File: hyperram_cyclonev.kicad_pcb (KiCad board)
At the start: 2 copper layers, 69 parts, among them IC1 AP63205WU, IC2 TXB0108PWR, IC3 S26KL128SDABHI020, IC4 W25Q32JVSSIQ_TR, IC5 S27KL0641DABHI020, J1 ASP-122952-01, J2 HDMI_A, J3 1156915, J4 1156915, J5 Conn_02x06_Top_Bottom, J6 Conn_02x06_Top_Bottom, J7 Conn_02x06_Top_Bottom, J8 1156915, J9 1156915, Q1 BSS138, Q2 BSS138

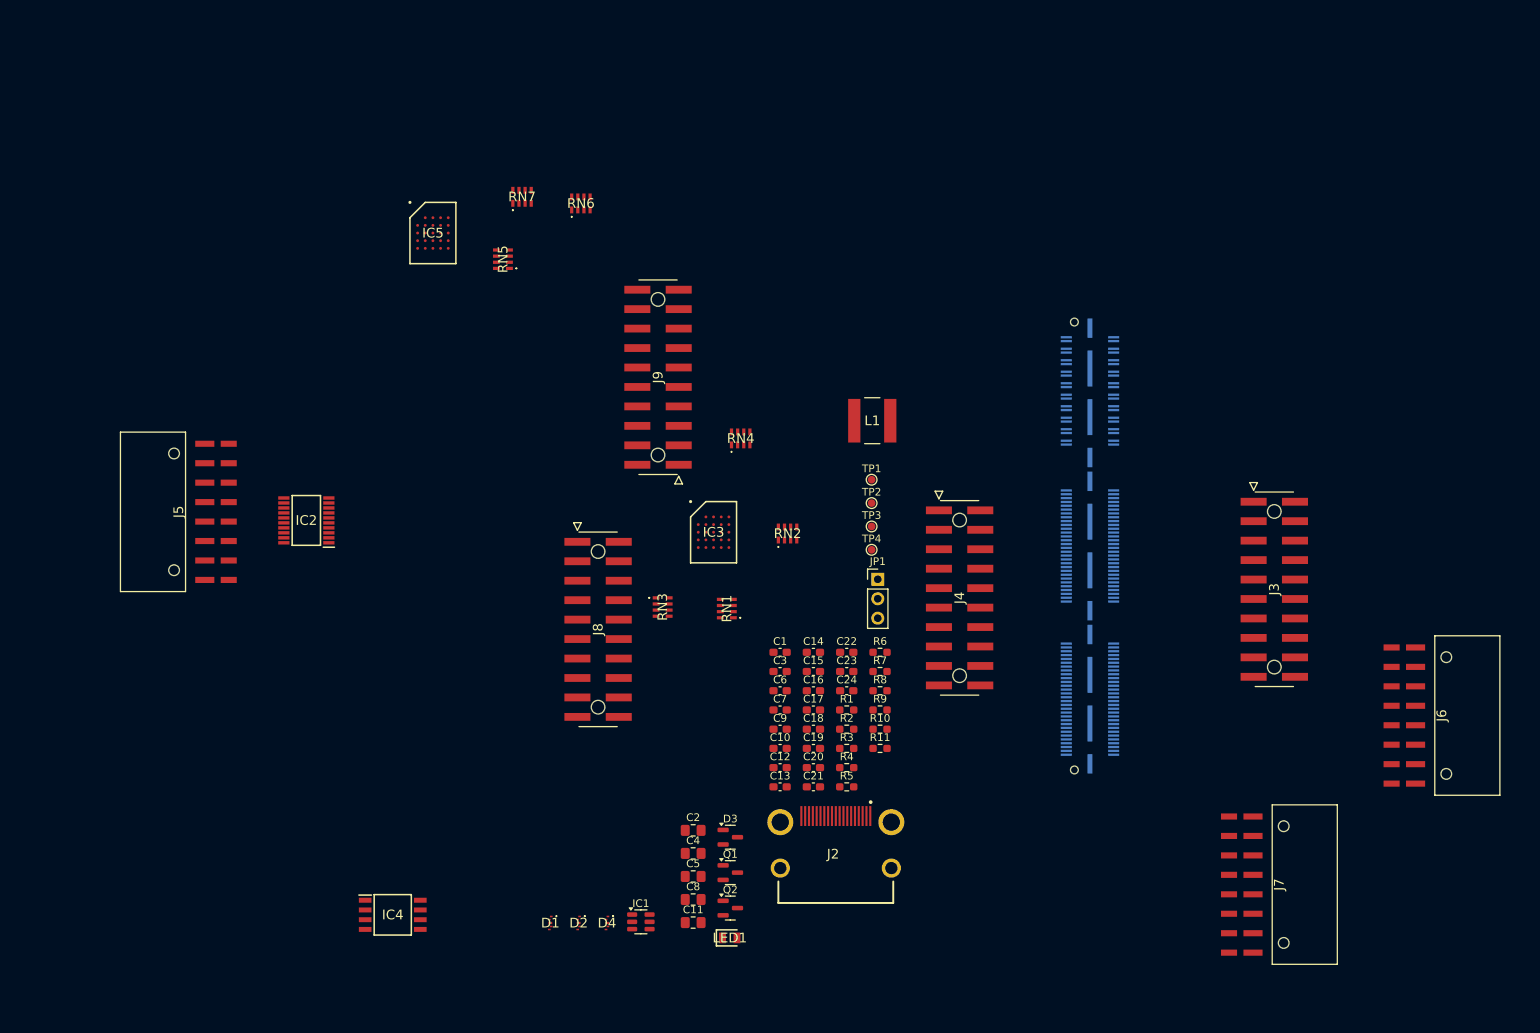
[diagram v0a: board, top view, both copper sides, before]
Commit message: Created edge.cuts. Updated PCB from schematic.
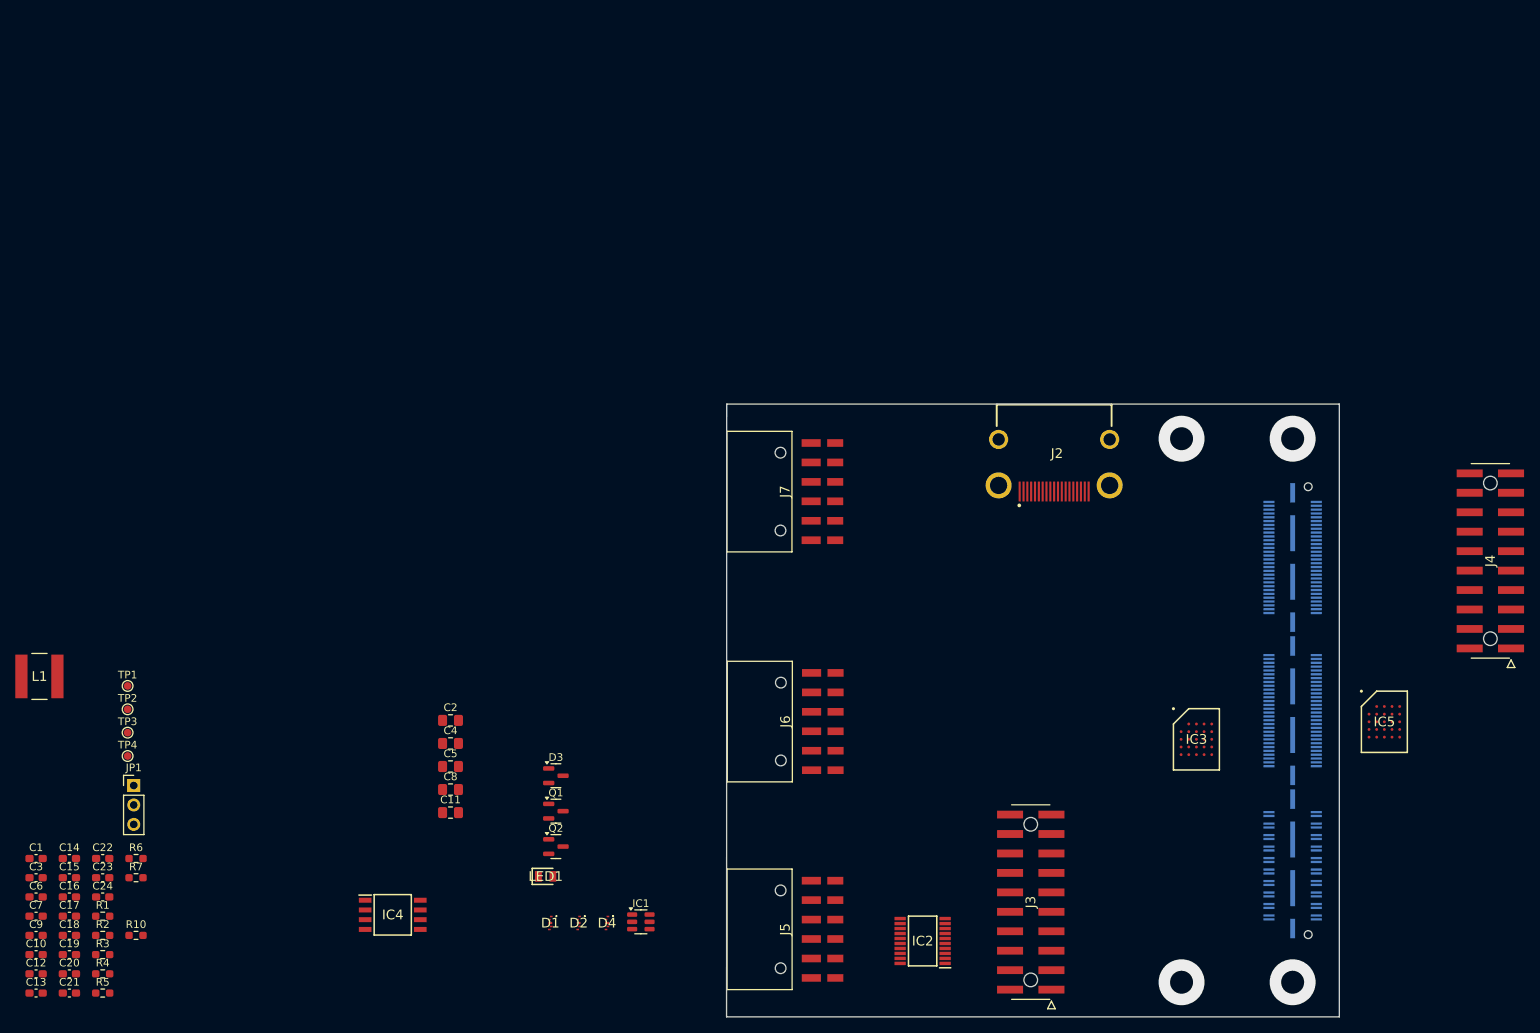
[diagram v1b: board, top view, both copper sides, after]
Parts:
- removed J8, J9: 1156915, hyperram_cyclonev:1156915
- removed R11, R8, R9: R, Resistor_SMD:R_0603_1608Metric_Pad0.98x0.95mm_HandSolder
- removed RN1, RN2, RN3, RN4, RN5, RN6, RN7: CAY16-22R0F4LF, hyperram_cyclonev:CAY16000J4LF
- moved IC5 139.7 mm to (234.5, 114.6)
- moved L1 113.7 mm to (58.9, 108.7)
- moved C1 100.8 mm to (58.4, 132.5)
- moved C10 100.8 mm to (58.4, 145.0)
- moved C12 100.8 mm to (58.4, 147.5)
- moved C13 100.8 mm to (58.4, 150.1)
- moved C14 100.8 mm to (62.8, 132.5)
- moved C15 100.8 mm to (62.8, 135.0)
- moved C16 100.8 mm to (62.8, 137.5)
- moved C17 100.8 mm to (62.8, 140.0)
- moved C18 100.8 mm to (62.8, 142.5)
- moved C19 100.8 mm to (62.8, 145.0)
- moved C20 100.8 mm to (62.8, 147.5)
- moved C21 100.8 mm to (62.8, 150.1)
- moved C22 100.8 mm to (67.1, 132.5)
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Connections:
- J1 pad 41: /cv_hf_csn -> /hf_csn
- J1 pad 42: /cv_hr2_csn -> /hr2_csn
- J1 pad 43: /cv_hr2_rstn -> /hr2_rstn
- J1 pad 44: /cv_hr2_rwds -> /hr2_rwds
- J1 pad 47: /cv_hf_rston -> /hf_rston
- J1 pad 48: /cv_hr2_dq7 -> /hr2_dq7
- J1 pad 49: /cv_hf_intn -> /hf_intn
- J1 pad 50: /cv_hr2_dq6 -> /hr2_dq6
- J1 pad 53: /cv_hr1_csn -> /hr1_csn
- J1 pad 54: /cv_hr2_dq5 -> /hr2_dq5
- J1 pad 55: /cv_hr1_rwds -> /hr1_rwds
- J1 pad 56: /cv_hr2_dq4 -> /hr2_dq4
- J1 pad 59: /cv_hr1_dq7 -> /hr1_dq7
- J1 pad 60: /cv_hr2_dq3 -> /hr2_dq3
- J1 pad 61: /cv_hr1_dq6 -> /hr1_dq6
- J1 pad 62: /cv_hr2_dq2 -> /hr2_dq2
- J1 pad 65: /cv_hr1_dq5 -> /hr1_dq5
- J1 pad 66: /cv_hr2_dq1 -> /hr2_dq1
- J1 pad 67: /cv_hr1_dq4 -> /hr1_dq4
- J1 pad 68: /cv_hr2_dq0 -> /hr2_dq0
- J1 pad 71: /cv_hr1_dq3 -> /hr1_dq3
- J1 pad 72: /cv_hr2_clkp -> /hr2_clkp
- J1 pad 73: /cv_hr1_dq2 -> /hr1_dq2
- J1 pad 74: /cv_hr2_clkn -> /hr2_clkn
- J1 pad 77: /cv_hr1_dq1 -> /hr1_dq1
- J1 pad 78: /cv_hf_psc -> /hf_psc
- J1 pad 79: /cv_hr1_dq0 -> /hr1_dq0
- J1 pad 80: /cv_hf_pscn -> /hf_pscn
- J1 pad 83: /cv_hr1_clkp -> /hr1_clkp
- J1 pad 85: /cv_hr1_clkn -> /hr1_clkn
- J1 pad 89: /cv_hr1_rstn -> /hr1_rstn
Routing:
- net (no net): vias 0 -> 4
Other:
- board outline added: 80 x 80 mm

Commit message: Fixed issue with PMOD pins assignment
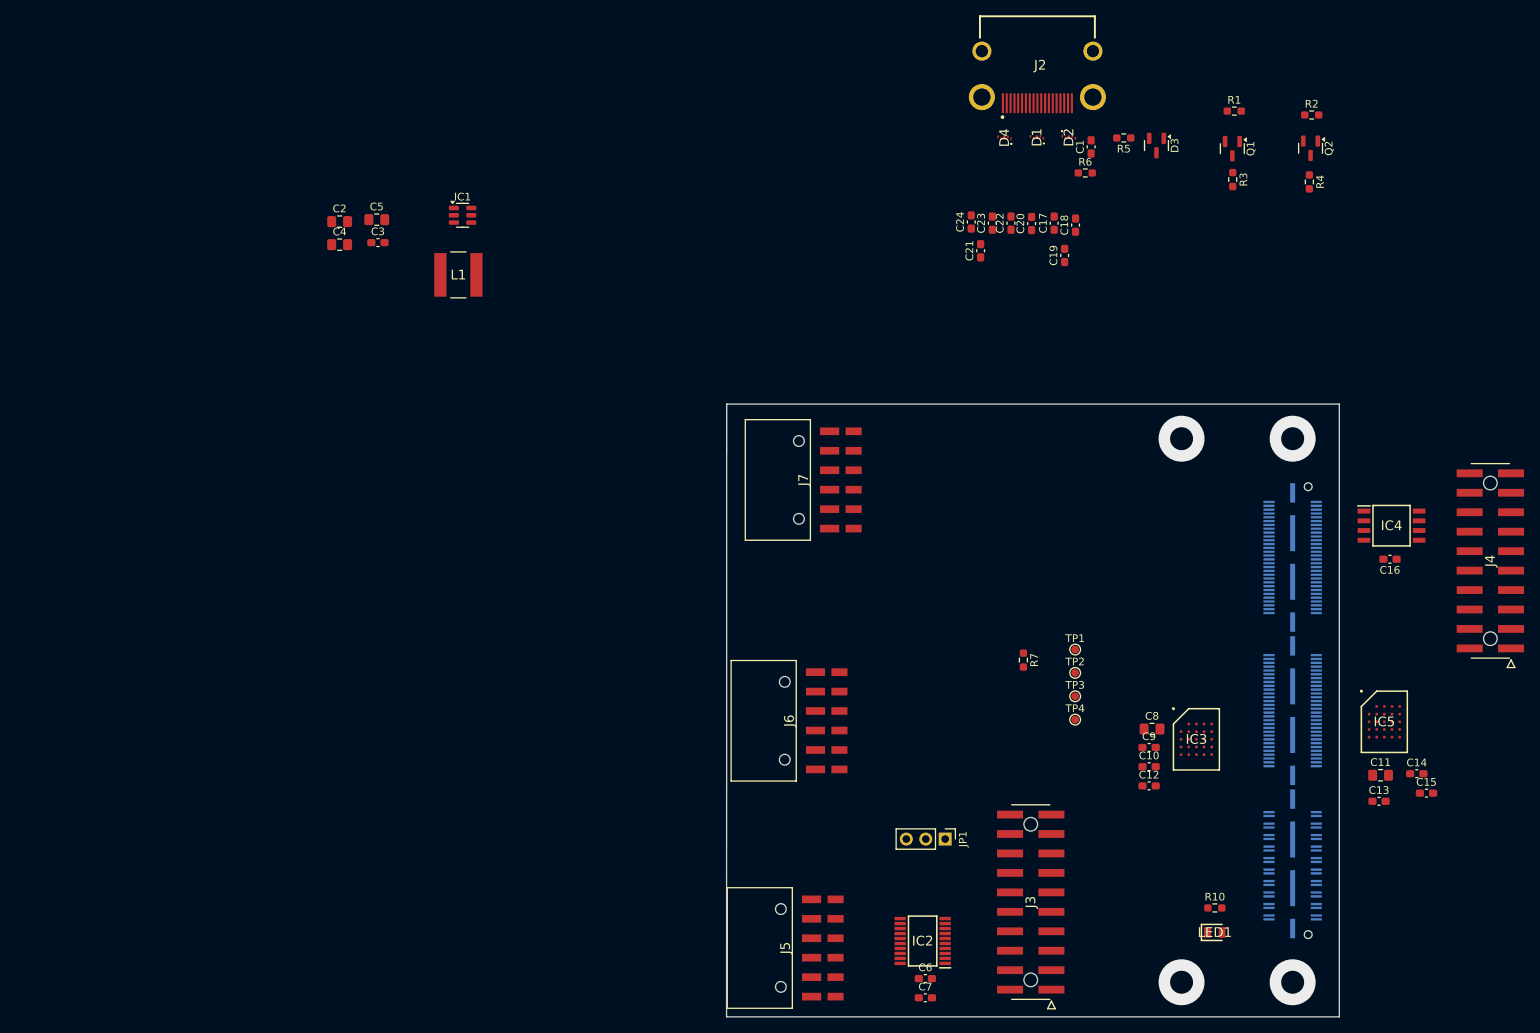
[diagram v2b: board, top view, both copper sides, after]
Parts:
- J5, J6, J7: value Conn_02x06_Top_Bottom -> Conn_02x06_Odd_Even
- moved R2 190.8 mm to (225.0, 35.4)
- moved R4 188.5 mm to (224.7, 44.1), turned to -90 degrees
- moved R1 181.3 mm to (214.9, 34.9)
- moved R3 178.9 mm to (214.7, 43.8), turned to -90 degrees
- moved C16 178.0 mm to (235.2, 93.4), turned to 180 degrees
- moved C15 177.5 mm to (240.0, 124.0)
- moved C13 177.1 mm to (233.8, 125.0)
- moved C14 176.3 mm to (238.7, 121.4)
- moved R5 173.9 mm to (200.5, 38.4), turned to 180 degrees
- moved C1 166.2 mm to (196.2, 39.6), turned to 90 degrees
- moved C18 160.8 mm to (194.2, 49.8), turned to 90 degrees
- moved C20 159.3 mm to (188.4, 49.6), turned to 90 degrees
- moved C19 158.8 mm to (192.7, 53.7), turned to 90 degrees
- moved C17 157.2 mm to (191.4, 49.5), turned to 90 degrees
- moved C21 153.5 mm to (181.8, 53.1), turned to 90 degrees
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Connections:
- J5 pad 1: /pmod5_io0 -> /pmod5_io6
- J5 pad 10: /pmod5_io7 -> GND
- J5 pad 11: GND -> VCCQ
- J5 pad 2: /pmod5_io1 -> /pmod5_io7
- J5 pad 3: /pmod5_io2 -> /pmod5_io4
- J5 pad 4: /pmod5_io3 -> /pmod5_io5
- J5 pad 5: GND -> /pmod5_io2
- J5 pad 6: VCCQ -> /pmod5_io3
- J5 pad 7: /pmod5_io4 -> /pmod5_io0
- J5 pad 8: /pmod5_io5 -> /pmod5_io1
- J5 pad 9: /pmod5_io6 -> GND
- J6 pad 1: /pmod3_io0n -> /pmod3_io3n
- J6 pad 10: /pmod3_io3p -> GND
- J6 pad 11: GND -> +3V3
- J6 pad 2: /pmod3_io0p -> /pmod3_io3p
- J6 pad 3: /pmod3_io1n -> /pmod3_io2n
- J6 pad 4: /pmod3_io1p -> /pmod3_io2p
- J6 pad 5: GND -> /pmod3_io1n
- J6 pad 6: +3V3 -> /pmod3_io1p
- J6 pad 7: /pmod3_io2n -> /pmod3_io0n
- J6 pad 8: /pmod3_io2p -> /pmod3_io0p
- J6 pad 9: /pmod3_io3n -> GND
- J7 pad 1: /pmod3_io4n -> /pmod3_io7n
- J7 pad 10: /pmod3_io7p -> GND
- J7 pad 11: GND -> +3V3
- J7 pad 2: /pmod3_io4p -> /pmod3_io7p
- J7 pad 3: /pmod3_io5n -> /pmod3_io6n
- J7 pad 4: /pmod3_io5p -> /pmod3_io6p
- J7 pad 5: GND -> /pmod3_io5n
- J7 pad 6: +3V3 -> /pmod3_io5p
- J7 pad 7: /pmod3_io6n -> /pmod3_io4n
- J7 pad 8: /pmod3_io6p -> /pmod3_io4p
- J7 pad 9: /pmod3_io7n -> GND

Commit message: Adjusted PCB dimensions. Moved components to the back side
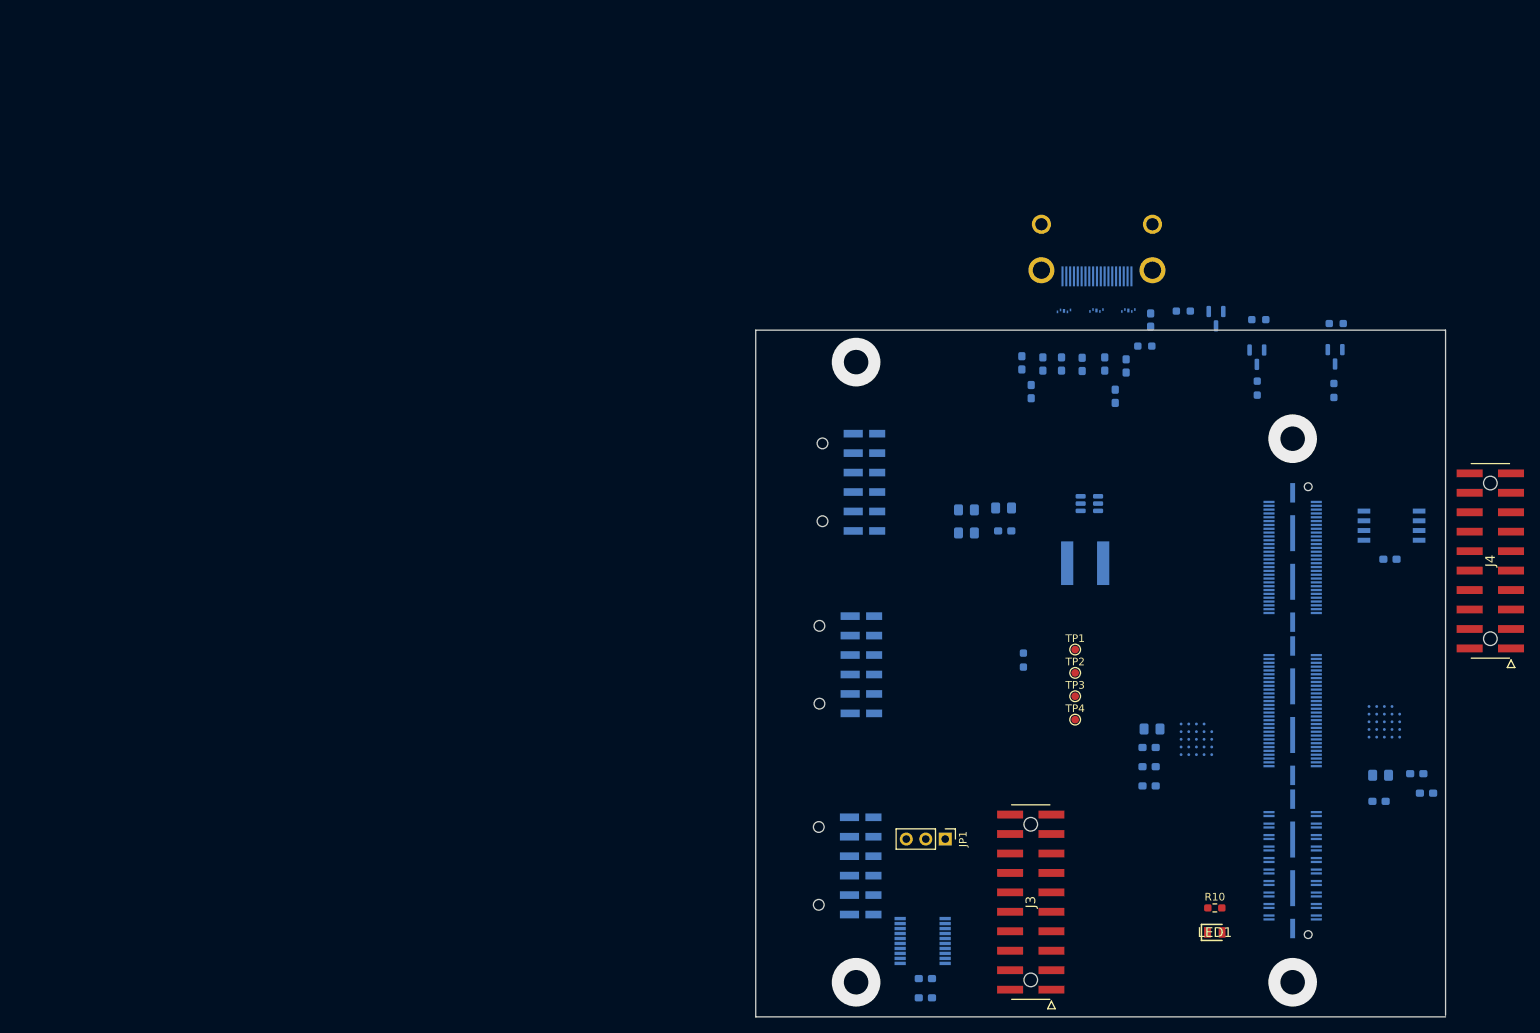
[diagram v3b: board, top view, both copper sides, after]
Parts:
- C1, C10, C11, C12, C13, C14, C15, C16, C17, C18, C19, C2, C20, C21, C22, C23, C24, C3, C4, C5, C6, C7, C8, C9, D1, D2, D3, D4, IC1, IC2, IC3, IC4, IC5, J2, J5, J6, J7, L1, Q1, Q2, R1, R2, R3, R4, R5, R6, R7: moved to B.Cu
- moved C2 90.1 mm to (179.9, 87.0), turned to 180 degrees
- moved C4 90.1 mm to (179.9, 90.0), turned to 180 degrees
- moved IC1 90.1 mm to (196.0, 86.1), turned to 180 degrees
- moved L1 90.1 mm to (195.4, 93.9), turned to 0 degrees
- moved C3 90.1 mm to (184.9, 89.7), turned to 180 degrees
- moved C5 90.1 mm to (184.8, 86.7), turned to 180 degrees
- moved Q2 27.4 mm to (228.0, 67.0)
- moved R1 27.4 mm to (218.1, 62.1), turned to 180 degrees
- moved R2 27.4 mm to (228.2, 62.6), turned to 180 degrees
- moved Q1 27.4 mm to (217.8, 67.0)
- moved R3 27.4 mm to (217.9, 71.1)
- moved R4 27.4 mm to (227.9, 71.4)
- moved D1 23.9 mm to (196.9, 60.9)
- moved D2 23.9 mm to (201.1, 60.9)
- moved D3 23.9 mm to (212.5, 62.0)
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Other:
- board size 80 x 80 mm -> 90.1 x 89.7 mm
